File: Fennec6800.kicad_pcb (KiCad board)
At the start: 2 copper layers, 218 x 131.9 mm, 117 parts, among them J1 Barrel_Jack, J2 DB25_Male, J3 Conn_02x20_Odd_Even, J4 DB25_Male, Q1 2N3904-AP, SW1 SW_DIP_x06, SW2 SW_DIP_x06, SW3 SW_Push, SW4 SW_DPDT_x2, U1 74LS00, U10 74LS245, U11 MC6800, U12 74LS244, U13 74LS244, U14 74LS244, U15 74LS138, U16 74LS138, U17 P2114, U18 P2114, U19 P2114, U2 74LS04, U20 P2114, U21 2716, U22 P2114, U23 P2114, U24 P2114, U25 P2114, U26 P2114, U27 P2114, U28 P2114, U29 P2114, U3 74LS193, U30 P2114, U31 P2114, U32 P2114, U33 P2114, U34 MAX232, U35 MAX232, U36 74LS30, U37 NE555P, U4 74LS73, U5 74LS02, U6 74LS74, U7 MC6850, U8 MC6850, U9 74LS245, X1 ACO-1.8432MHz

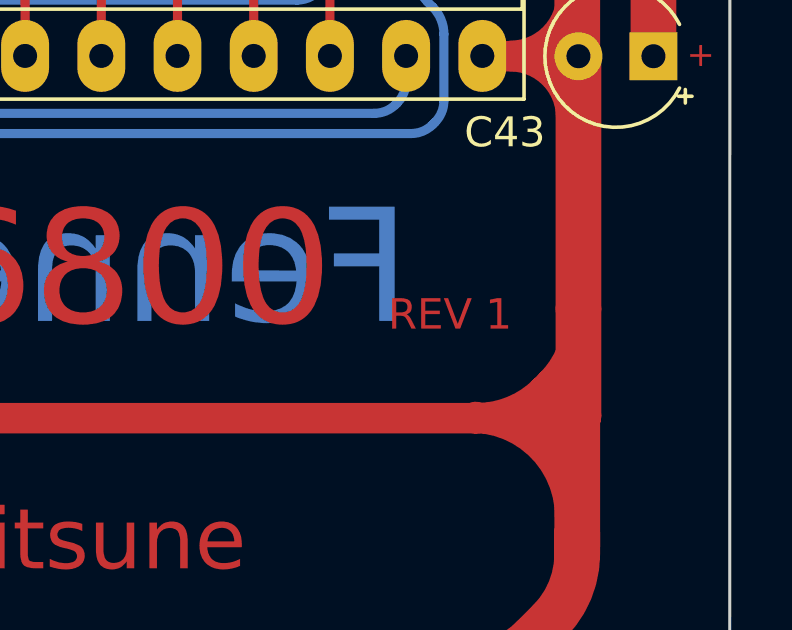
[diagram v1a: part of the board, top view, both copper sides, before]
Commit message: Reverted ref designator on PCB as bodge fixes are not yet done
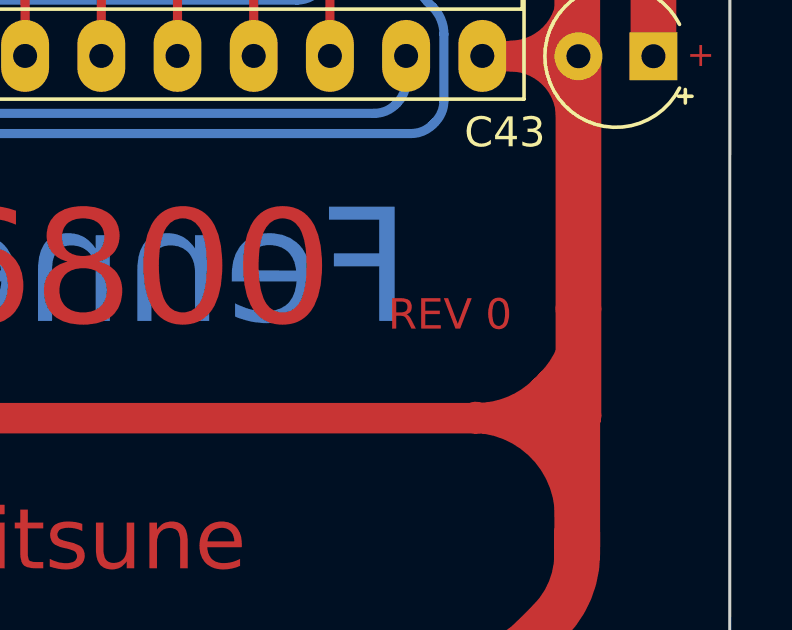
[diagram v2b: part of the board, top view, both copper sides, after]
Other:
- board text added: "REV 0"
- board text removed: "REV 1"
